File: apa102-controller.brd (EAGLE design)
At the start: 94.6 x 75.9 mm, 166 parts, among them IC1 REG1117, IC3 IC_MCP7940M-SOIC8, J1 DCJ0202, U1 ATMEGA328P, U2 74HC04_HEX_INVERTERSOIC, U3 24AA32A-I/MS, U4 ATMEGA328P, U5 TEXAS-INSTRUMENTS_BY_ELEMENT1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

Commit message: more labels
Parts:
- added LED12: CBUS0, adafruit:CHIP-LED0805
- added R28: 1k, rcl:R0805
- C1: value 10 -> 1u
- C2: value 100 -> 100n
- LED1: value (none) -> PWR-5MM
- LED9: value (none) -> PPS
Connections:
- net ADC1 renamed ADC1_TRIMPOT
- net ADC2 renamed ADC2_TRIMPOT
- net ARD_D4 renamed ARD_D4_GPS_EN
- net ARD_D9 renamed D9_LED_RED
- net D5 renamed D5_LED_GREEN
- net D6 renamed D6_LED_WHITE
- net DMINUS renamed UBLOX_DMINUS
- net DPLUS renamed UBLOX_DPLUS
- net N$12 renamed GPS_SDA
- net N$49 renamed WIREPAD_D8
- net N$55 renamed FT_DM
- net N$56 renamed FT_DP
- net N$6 renamed WIREPAD_D7
- net N$7 renamed UBLOX_RF_IN
- net N$8 renamed VCC_RF_2
- net RESET_PIN renamed ISP_RESET
- net SCL renamed ARD_SCK
- net SDI_ONE renamed ARD_MOSI
- removed net GND1: U$21.3
- removed net GND2: U$21.13
- removed net GND3: U$21.C
- removed net N$10: C44.1, C49.1, R11.2, U$21.1, U$21.8, U$21.9
- new net FT230_VCCIO: C44.1, C49.1, R11.2, R28.2, U$21.1, U$21.8, U$21.9
- new net FT_CB0: LED12.C, U$21.12
- new net N$58: LED12.A, R28.1
- net GND: now also U$21.13, U$21.3, U$21.C
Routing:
- net FT230_VCCIO: track 0.00 -> 30.9 mm, vias 0 -> 2
- net N$10: track 25.5 -> 0.00 mm
- net FT_CB0: track 0.00 -> 13.0 mm
- net GND: track 191.6 -> 197.8 mm, vias 192 -> 193
- net MEGATXD: track 36.6 -> 33.0 mm
- net N$58: track 0.00 -> 3.08 mm
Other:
- board text added: "CB0"
- board text added: "NEO 6M/Q 7M/Q"
- board text removed: "NEO 6M/Q"

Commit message: pcbs 20170206
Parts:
- removed SJ1: (no value), jumper:SJ
- moved D6 41.2 mm to (58.9, 6.35)
- moved JP3 0.25 mm to (74.3, 5.46)
- moved C17 0.25 mm to (32.9, 55.2)
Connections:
- removed net N$25: SJ1.2, U1.20
- net +5V: no longer SJ1.1
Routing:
- net +5V: track 313.9 -> 325.9 mm
- net N$25: track 2.28 -> 0.00 mm
- net RESET_328: track 72.2 -> 73.5 mm
- net GND: track 197.8 -> 196.9 mm
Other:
- board text added: "gitlab.com/apa102-controller"
- board text removed: "AREF"

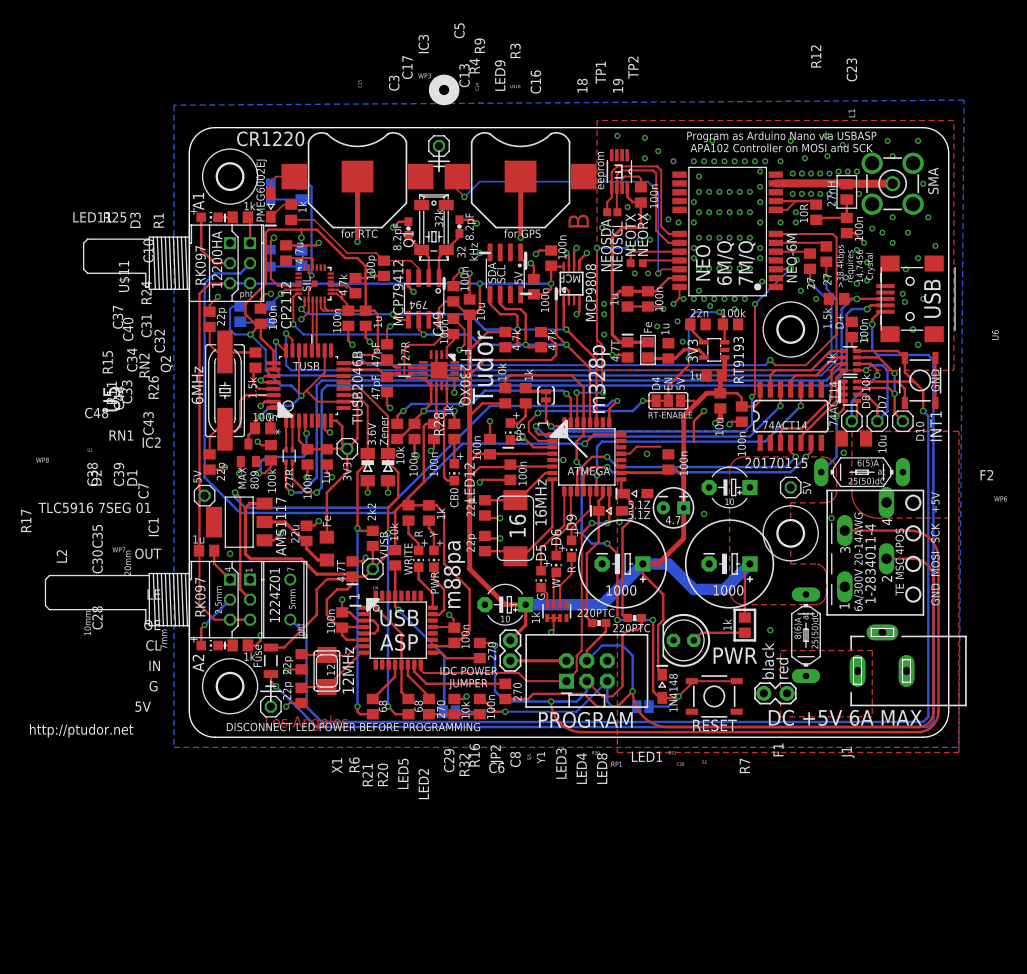
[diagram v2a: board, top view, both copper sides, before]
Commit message: add 1N4733 Zener
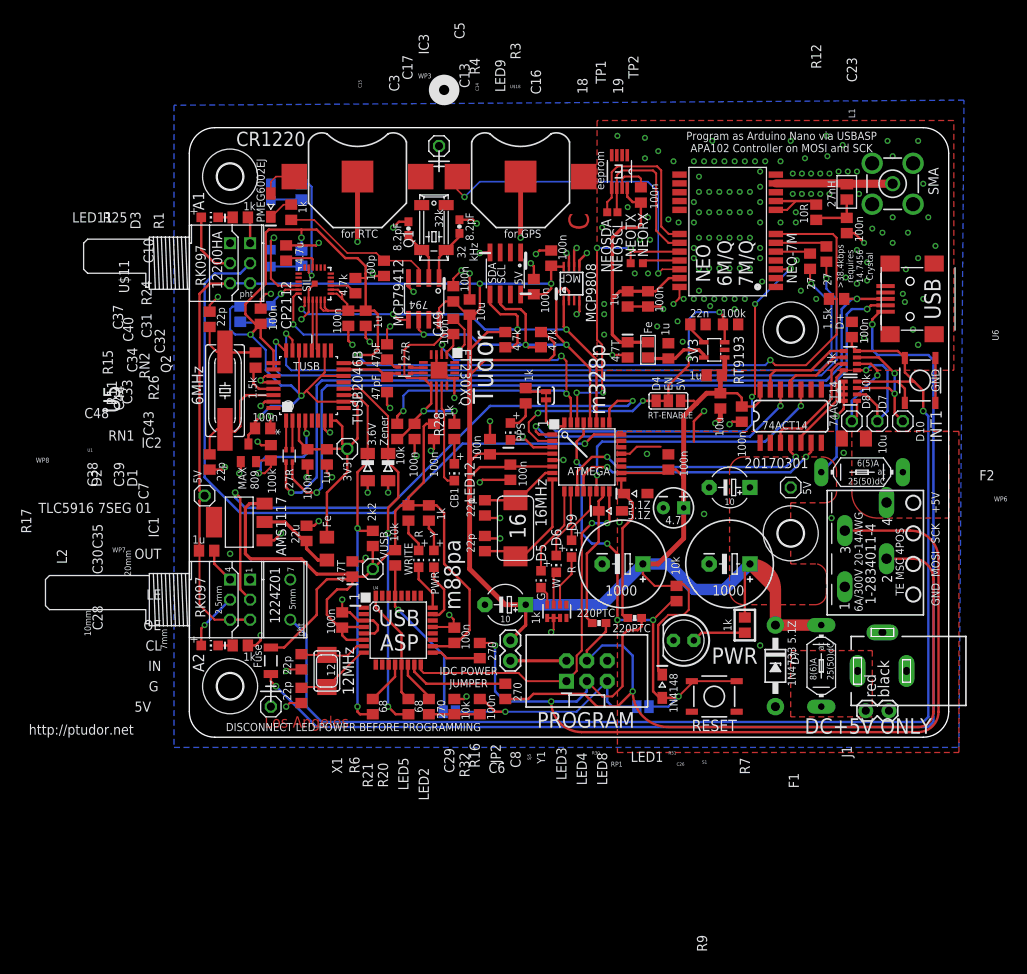
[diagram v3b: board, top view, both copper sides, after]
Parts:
- added D7: (no value), diode:DO41Z10
- D1, D2: device diode:MINIMELF -> diode:MINIMELF@1
- D3, D4, D5, D6: device diode:SOD323-W -> diode:SOD323-W@1
- LED12: value CBUS0 -> CBUS1
- moved R9 32.6 mm to (60.7, 17.9), turned to 270 degrees
- moved JP3 10.4 mm to (84.5, 3.30), turned to 0 degrees
- moved F1 4.26 mm to (78.7, 8.89)
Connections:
- net N$26 renamed USB_RAW_5V
- net +5V: now also D7.C
- net FT_CB0: now also U$21.11; no longer U$21.12
- net GND: now also D7.A
- net MEGATXD: now also U$21.2; no longer U$21.15
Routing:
- net +5V: track 325.9 -> 346.0 mm
- net MEGATXD: track 33.0 -> 50.7 mm, vias 3 -> 4
- net RESET_328: track 73.5 -> 61.4 mm
- net ADC2_TRIMPOT: track 71.5 -> 75.3 mm
- net GND: track 196.9 -> 197.6 mm
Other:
- board text added: "1N4733 5.1Z"
- board text added: "20170301"
- board text added: "C"
- board text added: "CB1"
- board text added: "DC+5V ONLY"
- board text added: "NEO-7M"
- board text removed: "20170115"
- board text removed: "B"
- board text removed: "CB0"
- board text removed: "DC +5V 6A MAX"
- board text removed: "NEO-6M"

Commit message: labels
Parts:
- added C52: 100nF, rcl:C0805
- added U$23: ESDTUDOR, adafruit:SOT23-5L
- moved R12 1.27 mm to (79.4, 65.4)
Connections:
- net CP_DMINUS_TI renamed USB_CP_DMINUS_A
- net CP_DPLUS_TI renamed USB_CP_DPLUS_A
- net DMINUS_ASP renamed USB_ASP_DMINUS_A
- net DMINUS_HUB renamed USB_HUB_DMINUS_A
- net DMINUS_NEO_END renamed USB_NEO_DMINUS_B
- net DPLUS_ASP renamed USB_ASP_DPLUS_A
- net DPLUS_HUB renamed USB_HUB_DPLUS_A
- net DPLUS_NEO_END renamed USB_NEO_DPLUS_B
- net FT-DMINUS renamed USB_FT_DMINUS_B
- net FT-DPLUS renamed USB_FT_DPLUS_B
- net FT_DM renamed USB_FT_DMINUS_A
- net FT_DP renamed USB_FT_DPLUS_A
- net N$37 renamed USB_ASP_DPLUS_B
- net N$38 renamed USB_ASP_DMINUS_B
- net TUSB_DMINUS_POSTRES renamed USB_HUB_DMINUS_B
- net TUSB_DPLUS_POSTRES renamed USB_HUB_DPLUS_B
- net UBLOX_DMINUS renamed USB_NEO_DMINUS_A
- net UBLOX_DPLUS renamed USB_NEO_DPLUS_A
- net GND: now also C52.2
- net USB-3V3: now also C52.1
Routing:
- net USB_NEO_DMINUS_B: track 87.5 -> 90.0 mm
- net VCC_RF_2: track 6.35 -> 5.08 mm
- net VCC_RF: track 8.27 -> 9.54 mm
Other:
- board text added: "27 nH"
- board text removed: "27nH"
